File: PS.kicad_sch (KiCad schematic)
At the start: 26 parts, among them U15 MIC26903YJL-TR, U16 OPA2196xDGK

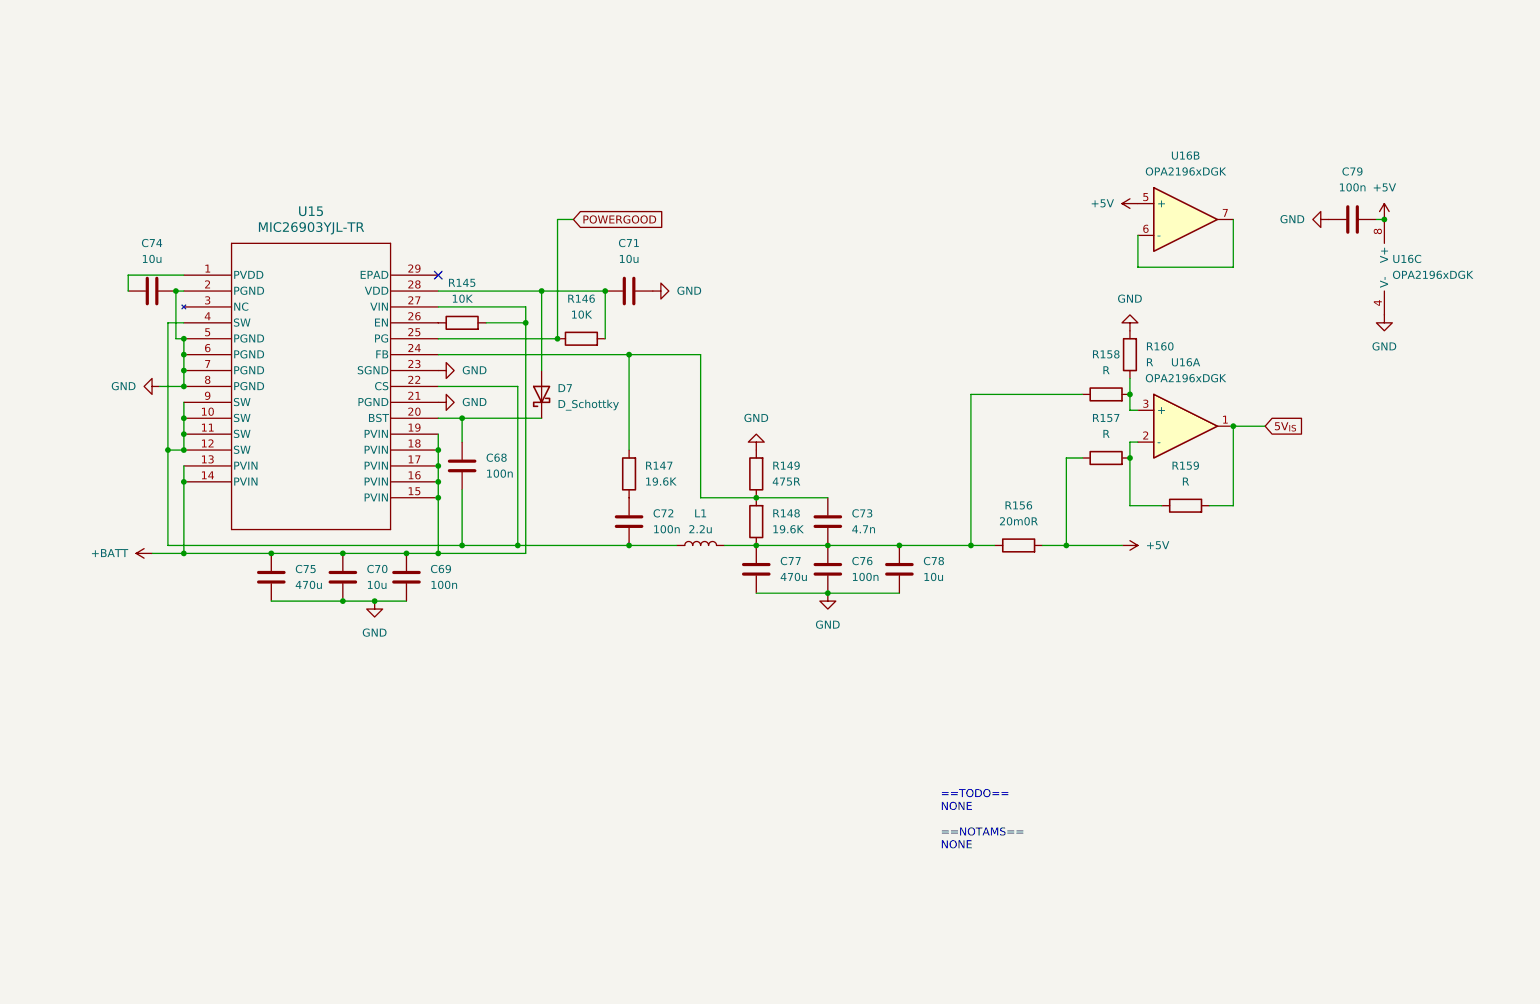
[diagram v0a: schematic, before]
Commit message: The great decluttering
Moved all possible controls to I2C, part selection commenced, IOs assigned pending comms schema
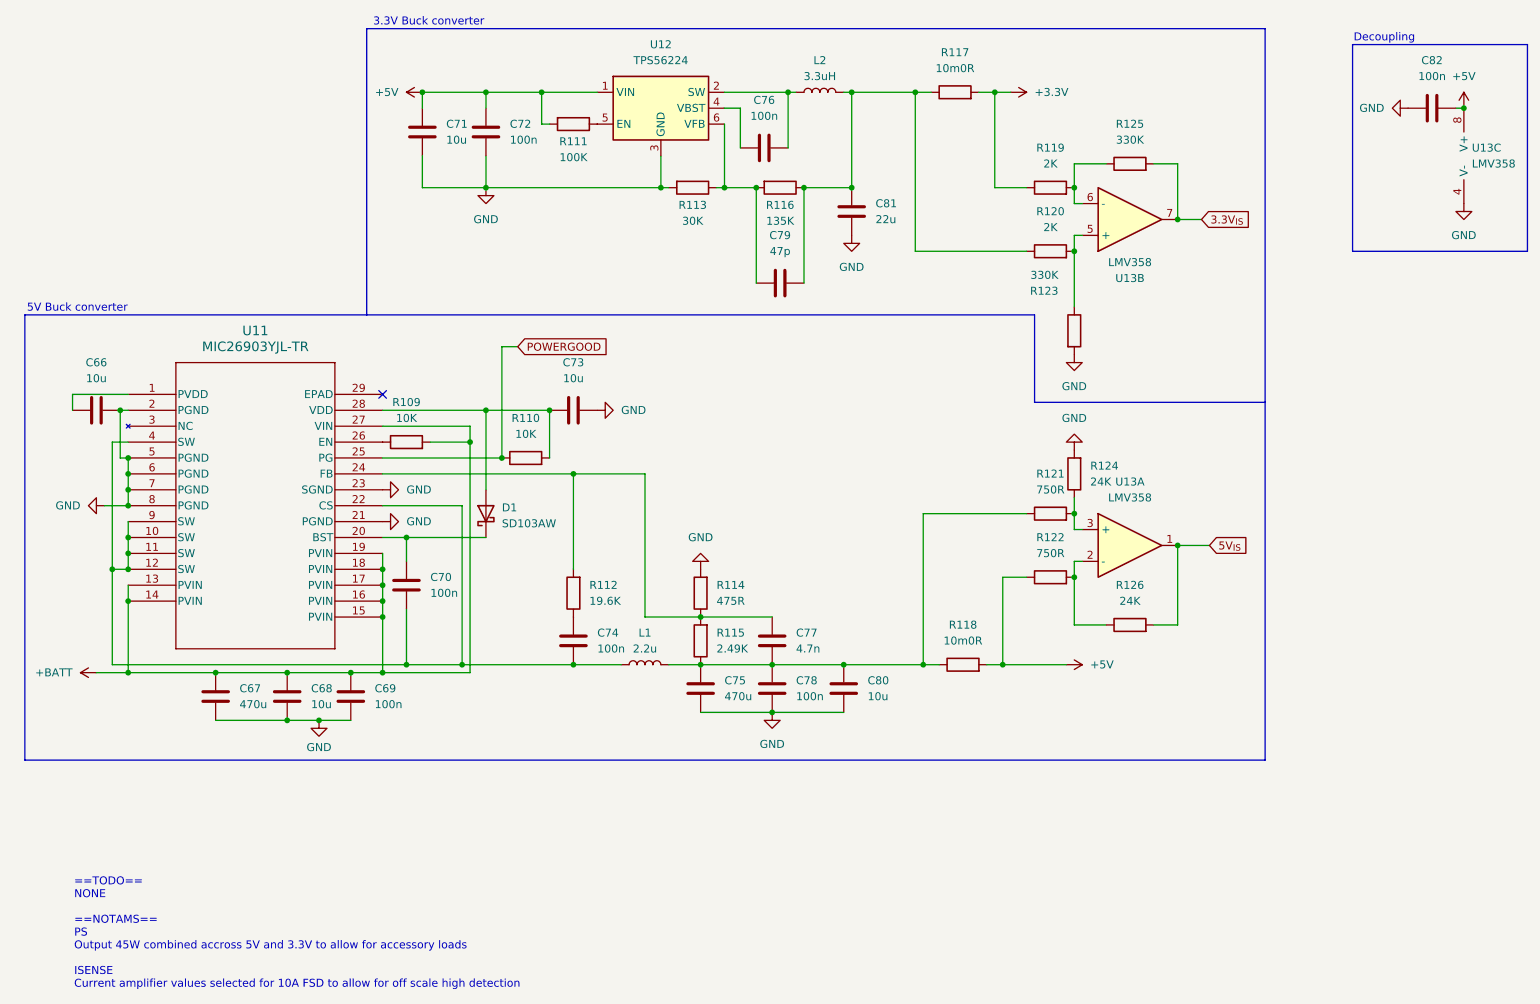
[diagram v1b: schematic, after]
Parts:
- added C71: 10u, Capacitor_SMD:C_0603_1608Metric, symbol Device:C
- added C72, C76: 100n, Capacitor_SMD:C_0603_1608Metric, symbol Device:C
- added C79: 47p, Capacitor_SMD:C_0603_1608Metric, symbol Device:C
- added C81: 22u, Capacitor_SMD:C_0603_1608Metric, symbol Device:C
- added L2: 3.3uH, Inductor_SMD:L_Coilcraft_LPS3314, symbol Device:L
- added R111: 100K, Resistor_SMD:R_0603_1608Metric, symbol Device:R
- added R113: 30K, Resistor_SMD:R_0603_1608Metric, symbol Device:R
- added R116: 135K, Resistor_SMD:R_0603_1608Metric, symbol Device:R
- added R117: 10m0R, Resistor_SMD:R_Shunt_Isabellenhuette_BVR4026, symbol Device:R
- added R119, R120: 2K, Resistor_SMD:R_0603_1608Metric, symbol Device:R
- added R123, R125: 330K, Resistor_SMD:R_0603_1608Metric, symbol Device:R
- added U12: TPS56224, Package_TO_SOT_SMD:SOT-563, symbol Regulator_Switching:TPS562202
- D1: renamed from D7; value D_Schottky -> SD103AW; footprint Diode_SMD:D_0603_1608Metric -> Diode_SMD:D_SOD-123
- R115: renamed from R148; value 19.6K -> 2.49K
- R118: renamed from R156; value 20m0R -> 10m0R; footprint Resistor_SMD:R_2816_7142Metric_Pad3.20x4.45mm_HandSolder -> Resistor_SMD:R_Shunt_Isabellenhuette_BVR4026
- R121: renamed from R158; value R -> 750R
- R122: renamed from R157; value R -> 750R
- R124: renamed from R160; value R -> 24K
- R126: renamed from R159; value R -> 24K
- U13: renamed from U16; value OPA2196xDGK -> LMV358
- renumbered C74 to C66, C75 to C67, C70 to C68, C68 to C70, C71 to C73, C72 to C74, C77 to C75, C73 to C77, C76 to C78, C78 to C80, C79 to C82, R145 to R109, R146 to R110, R147 to R112, R149 to R114, U15 to U11
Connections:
- net +5V: now also C71.1, C72.1, R111.2, U12.1 (VIN); no longer U13.5 (+)
- net GND: now also C71.2, C72.2, C81.2, R113.2, R123.2, U12.3 (GND)
- net at U13.6 (-): now also R119.2, R125.1; no longer U13.7
- new net: C79.1, C81.1, L2.2, R116.1, R117.1, R120.1
- new net: C79.2, R113.1, R116.2, U12.6 (VFB)
- new net: R120.2, R123.1, U13.5 (+)
- new net: C76.1, L2.1, U12.2 (SW)
- new net: C76.2, U12.4 (VBST)
- new net: R111.1, U12.5 (EN)
- new net +3.3V: R117.2, R119.1
- new net 3.3V_{IS}: R125.2, U13.7
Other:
- note added: "3.3V Buck converter"
- note added: "5V Buck converter"
- note added: "==TODO== NONE ==NOTAMS== PS Output 45W combined accross 5V and 3.3V to allow for accessory loads ISENSE Current amplifier values selected for 10A FSD to allow for off scale high detection"
- note added: "Decoupling"
- note removed: "==TODO== NONE ==NOTAMS== NONE"
- moved on the sheet: C66, C67, C68, C69, C70, C73, C74, C75, C77, C78, C80, C82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

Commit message: Powerstage
Powerstage layout, non critical changes to schematic
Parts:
- removed R117, R118: 10m0R, Resistor_SMD:R_Shunt_Isabellenhuette_BVR4026, symbol Device:R
- added R117, R118: WSL3637R0100FEA, WSL3637_VIS, symbol WSL3637R0100FEA:WSL3637R0100FEA
- C66, C71, C73: footprint Capacitor_SMD:C_0603_1608Metric -> Capacitor_SMD:C_0402_1005Metric
- C70, C72, C76, C79, C82: footprint Capacitor_SMD:C_0603_1608Metric -> Capacitor_SMD:C_0201_0603Metric
- C77: value 4.7n -> ~; footprint Capacitor_SMD:C_0603_1608Metric -> Capacitor_SMD:C_0201_0603Metric
- L1: footprint (none) -> Inductor_SMD:L_Bourns_SRN8040TA
- renumbered D1 to D7
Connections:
- net +3.3V: now also R117.4; no longer R119.1
- net +5V: now also R118.1; no longer R122.1
- net GND: now also U11.29 (EPAD)
- net at C79.1, C81.1, L2.2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: now also R117.1; no longer R120.1
- net at C75.2, C77.2, C78.2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: now also R118.4; no longer R121.1
- new net: R118.3, R121.1
- new net: R117.2, R120.1
- new net: R118.2, R122.1
- new net: R117.3, R119.1
- no-connect marks 1 -> 0
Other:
- moved on the sheet: R123
